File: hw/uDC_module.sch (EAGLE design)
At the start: 38 parts, among them J1 GROVE-4P-2.0-3470130P1, J2 GROVE-4P-2.0-3470130P1, U5 LD3985XX, X1 22-23-2021, X2 22-23-2021, X3 53047-06, X4 53047-06

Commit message: layout completed
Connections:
- new net ANALOG: U$6.PA2, X4-6.S
- new net ENC_A: U$6.PB6, X4-3.S
- new net ENC_B: U$6.PB7, X4-4.S
- new net ENC_I: U$6.PB5, X4-5.S
- new net LIMIT_A: U$6.PA3, X3-1.S
- new net LIMIT_B: U$6.PA4, X3-3.S
- new net STOP: U$6.PA5, X3-5.S
- net +5V: now also X4-1.S
- net GND: now also X3-2.S, X3-4.S, X3-6.S, X4-2.S
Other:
- moved on the sheet: X3-1, X3-2, X3-3, X3-4, X3-5, X3-6
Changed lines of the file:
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@@
 <part name="ZD1" library="dp_devices" deviceset="ZENER" device="SOD-323F"/>
 <part name="GND27" library="supply" deviceset="GND" device=""/>
+<part name="GND32" library="supply1" deviceset="GND" device=""/>
+<part name="P+4" library="supply" deviceset="+5V" device=""/>
+<part name="GND33" library="supply1" deviceset="GND" device=""/>
 </parts>
 <sheets>
@@
 <instance part="X2" gate="-1" x="317.5" y="127"/>
 <instance part="X2" gate="-2" x="317.5" y="124.46"/>
-<instance part="X3" gate="-1" x="271.78" y="124.46"/>
-<instance part="X3" gate="-2" x="271.78" y="121.92"/>
-<instance part="X3" gate="-3" x="271.78" y="119.38"/>
-<instance part="X3" gate="-4" x="271.78" y="116.84"/>
-<instance part="X3" gate="-5" x="271.78" y="114.3"/>
-<instance part="X3" gate="-6" x="271.78" y="111.76"/>
+<instance part="X3" gate="-1" x="281.94" y="109.22"/>
+<instance part="X3" gate="-2" x="281.94" y="106.68"/>
+<instance part="X3" gate="-3" x="281.94" y="104.14"/>
+<instance part="X3" gate="-4" x="281.94" y="101.6"/>
+<instance part="X3" gate="-5" x="281.94" y="99.06"/>
+<instance part="X3" gate="-6" x="281.94" y="96.52"/>
 <instance part="C12" gate="G$1" x="248.92" y="198.12"/>
 <instance part="GND18" gate="1" x="304.8" y="137.16"/>
@@
 <instance part="ZD1" gate="G$1" x="180.34" y="170.18" rot="R90"/>
 <instance part="GND27" gate="1" x="180.34" y="162.56"/>
+<instance part="GND32" gate="1" x="228.6" y="91.44"/>
+<instance part="P+4" gate="1" x="228.6" y="116.84"/>
+<instance part="GND33" gate="1" x="276.86" y="91.44"/>
 </instances>
 <busses>
@@
 <pinref part="GND27" gate="1" pin="GND"/>
 <wire x1="180.34" y1="167.64" x2="180.34" y2="165.1" width="0.1524" layer="91"/>
+</segment>
+<segment>
+<pinref part="X4" gate="-2" pin="S"/>
+<wire x1="231.14" y1="106.68" x2="228.6" y2="106.68" width="0.1524" layer="91"/>
+<wire x1="228.6" y1="106.68" x2="228.6" y2="93.98" width="0.1524" layer="91"/>
+<pinref part="GND32" gate="1" pin="GND"/>
+</segment>
+<segment>
+<pinref part="X3" gate="-2" pin="S"/>
+<wire x1="279.4" y1="106.68" x2="276.86" y2="106.68" width="0.1524" layer="91"/>
+<wire x1="276.86" y1="106.68" x2="276.86" y2="101.6" width="0.1524" layer="91"/>
+<pinref part="X3" gate="-4" pin="S"/>
+<wire x1="276.86" y1="101.6" x2="276.86" y2="96.52" width="0.1524" layer="91"/>
+<wire x1="276.86" y1="96.52" x2="276.86" y2="93.98" width="0.1524" layer="91"/>
+<wire x1="279.4" y1="101.6" x2="276.86" y2="101.6" width="0.1524" layer="91"/>
+<junction x="276.86" y="101.6"/>
+<pinref part="X3" gate="-6" pin="S"/>
+<wire x1="279.4" y1="96.52" x2="276.86" y2="96.52" width="0.1524" layer="91"/>
+<junction x="276.86" y="96.52"/>
+<pinref part="GND33" gate="1" pin="GND"/>
 </segment>
 </net>
@@
 <pinref part="P+3" gate="1" pin="+5V"/>
 </segment>
+<segment>
+<pinref part="X4" gate="-1" pin="S"/>
+<wire x1="231.14" y1="109.22" x2="228.6" y2="109.22" width="0.1524" layer="91"/>
+<wire x1="228.6" y1="109.22" x2="228.6" y2="114.3" width="0.1524" layer="91"/>
+<pinref part="P+4" gate="1" pin="+5V"/>
+</segment>
 </net>
 <net name="D1" class="0">
@@
 </segment>
 </net>
+<net name="ENC_A" class="0">
+<segment>
+<pinref part="X4" gate="-3" pin="S"/>
+<wire x1="231.14" y1="104.14" x2="226.06" y2="104.14" width="0.1524" layer="91"/>
+<label x="226.06" y="104.14" size="1.778" layer="95" rot="MR0"/>
+</segment>
+<segment>
+<pinref part="U$6" gate="G$1" pin="PB6"/>
+<wire x1="83.82" y1="208.28" x2="86.36" y2="208.28" width="0.1524" layer="91"/>
+<label x="86.36" y="208.28" size="1.778" layer="95"/>
+</segment>
+</net>
+<net name="ENC_B" class="0">
+<segment>
+<pinref part="X4" gate="-4" pin="S"/>
+<wire x1="231.14" y1="101.6" x2="226.06" y2="101.6" width="0.1524" layer="91"/>
+<label x="226.06" y="101.6" size="1.778" layer="95" rot="MR0"/>
+</segment>
+<segment>
+<pinref part="U$6" gate="G$1" pin="PB7"/>
+<wire x1="83.82" y1="210.82" x2="86.36" y2="210.82" width="0.1524" layer="91"/>
+<label x="86.36" y="210.82" size="1.778" layer="95"/>
+</segment>
+</net>
+<net name="ENC_I" class="0">
+<segment>
+<pinref part="X4" gate="-5" pin="S"/>
+<wire x1="231.14" y1="99.06" x2="226.06" y2="99.06" width="0.1524" layer="91"/>
+<label x="226.06" y="99.06" size="1.778" layer="95" rot="MR0"/>
+</segment>
+<segment>
+<pinref part="U$6" gate="G$1" pin="PB5"/>
+<wire x1="83.82" y1="205.74" x2="86.36" y2="205.74" width="0.1524" layer="91"/>
+<label x="86.36" y="205.74" size="1.778" layer="95"/>
+</segment>
+</net>
+<net name="ANALOG" class="0">
+<segment>
+<pinref part="X4" gate="-6" pin="S"/>
+<wire x1="231.14" y1="96.52" x2="226.06" y2="96.52" width="0.1524" layer="91"/>
+<label x="226.06" y="96.52" size="1.778" layer="95" rot="MR0"/>
+</segment>
+<segment>
+<pinref part="U$6" gate="G$1" pin="PA2"/>
+<wire x1="25.4" y1="195.58" x2="22.86" y2="195.58" width="0.1524" layer="91"/>
+<label x="22.86" y="195.58" size="1.778" layer="95" rot="MR0"/>
+</segment>
+</net>
+<net name="STOP" class="0">
+<segment>
+<pinref part="X3" gate="-5" pin="S"/>
+<wire x1="279.4" y1="99.06" x2="274.32" y2="99.06" width="0.1524" layer="91"/>
+<label x="274.32" y="99.06" size="1.778" layer="95" rot="MR0"/>
+</segment>
+<segment>
+<pinref part="U$6" gate="G$1" pin="PA5"/>
+<wire x1="43.18" y1="177.8" x2="43.18" y2="175.26" width="0.1524" layer="91"/>
+<label x="43.18" y="175.26" size="1.778" layer="95" rot="MR270"/>
+</segment>
+</net>
+<net name="LIMIT_B" class="0">
+<segment>
+<pinref part="X3" gate="-3" pin="S"/>
+<wire x1="279.4" y1="104.14" x2="274.32" y2="104.14" width="0.1524" layer="91"/>
+<label x="274.32" y="104.14" size="1.778" layer="95" rot="MR0"/>
+</segment>
+<segment>
+<pinref part="U$6" gate="G$1" pin="PA4"/>
+<wire x1="40.64" y1="177.8" x2="40.64" y2="175.26" width="0.1524" layer="91"/>
+<label x="40.64" y="175.26" size="1.778" layer="95" rot="MR270"/>
+</segment>
+</net>
+<net name="LIMIT_A" class="0">
+<segment>
+<pinref part="X3" gate="-1" pin="S"/>
+<wire x1="279.4" y1="109.22" x2="274.32" y2="109.22" width="0.1524" layer="91"/>
+<label x="274.32" y="109.22" size="1.778" layer="95" rot="MR0"/>
+</segment>
+<segment>
+<pinref part="U$6" gate="G$1" pin="PA3"/>
+<wire x1="25.4" y1="193.04" x2="22.86" y2="193.04" width="0.1524" layer="91"/>
+<label x="22.86" y="193.04" size="1.778" layer="95" rot="MR0"/>
+</segment>
+</net>

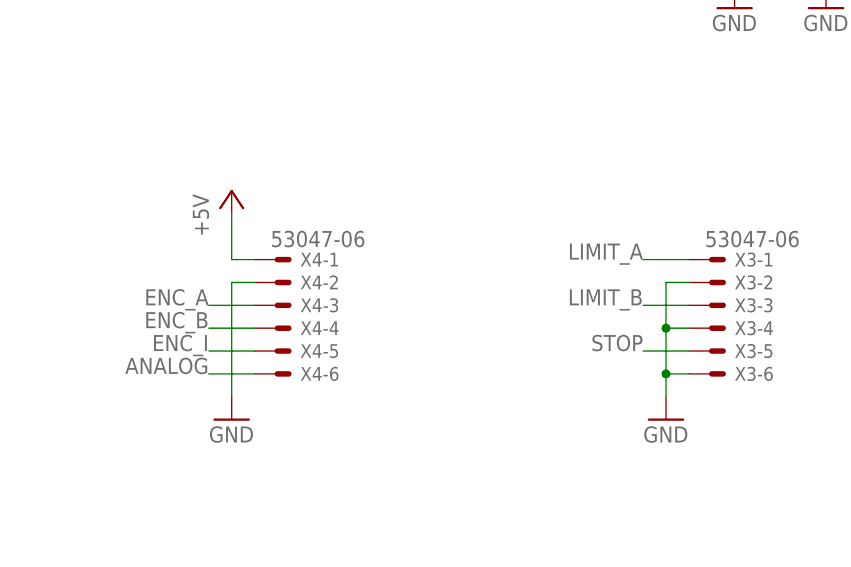
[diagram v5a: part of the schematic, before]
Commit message: updated all connectors to have GND on pin 1
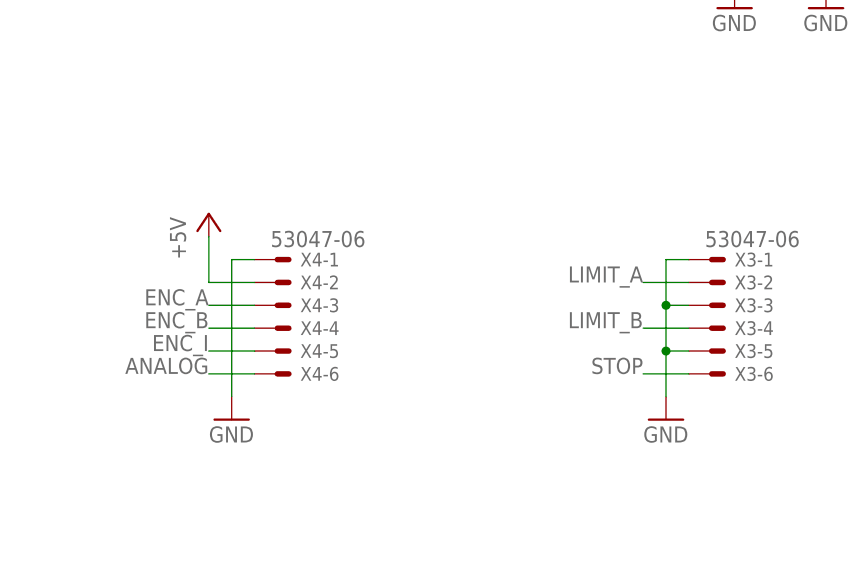
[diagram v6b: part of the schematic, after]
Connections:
- net +5V: now also X4-2.S; no longer X4-1.S
- net GND: now also X3-1.S, X3-3.S, X3-5.S, X4-1.S; no longer X3-2.S, X3-4.S, X3-6.S, X4-2.S
- net LIMIT_A: now also X3-2.S; no longer X3-1.S
- net LIMIT_B: now also X3-4.S; no longer X3-3.S
- net STOP: now also X3-6.S; no longer X3-5.S
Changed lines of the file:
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@@
 <instance part="GND27" gate="1" x="180.34" y="162.56"/>
 <instance part="GND32" gate="1" x="228.6" y="91.44"/>
-<instance part="P+4" gate="1" x="228.6" y="116.84"/>
+<instance part="P+4" gate="1" x="226.06" y="114.3"/>
 <instance part="GND33" gate="1" x="276.86" y="91.44"/>
 </instances>
@@
 </segment>
 <segment>
-<pinref part="X4" gate="-2" pin="S"/>
-<wire x1="231.14" y1="106.68" x2="228.6" y2="106.68" width="0.1524" layer="91"/>
 <wire x1="228.6" y1="106.68" x2="228.6" y2="93.98" width="0.1524" layer="91"/>
 <pinref part="GND32" gate="1" pin="GND"/>
-</segment>
-<segment>
-<pinref part="X3" gate="-2" pin="S"/>
-<wire x1="279.4" y1="106.68" x2="276.86" y2="106.68" width="0.1524" layer="91"/>
-<wire x1="276.86" y1="106.68" x2="276.86" y2="101.6" width="0.1524" layer="91"/>
-<pinref part="X3" gate="-4" pin="S"/>
-<wire x1="276.86" y1="101.6" x2="276.86" y2="96.52" width="0.1524" layer="91"/>
+<pinref part="X4" gate="-1" pin="S"/>
+<wire x1="231.14" y1="109.22" x2="228.6" y2="109.22" width="0.1524" layer="91"/>
+<wire x1="228.6" y1="109.22" x2="228.6" y2="106.68" width="0.1524" layer="91"/>
+</segment>
+<segment>
+<wire x1="276.86" y1="109.22" x2="276.86" y2="104.14" width="0.1524" layer="91"/>
+<wire x1="276.86" y1="104.14" x2="276.86" y2="101.6" width="0.1524" layer="91"/>
+<wire x1="276.86" y1="101.6" x2="276.86" y2="99.06" width="0.1524" layer="91"/>
+<wire x1="276.86" y1="99.06" x2="276.86" y2="96.52" width="0.1524" layer="91"/>
 <wire x1="276.86" y1="96.52" x2="276.86" y2="93.98" width="0.1524" layer="91"/>
-<wire x1="279.4" y1="101.6" x2="276.86" y2="101.6" width="0.1524" layer="91"/>
-<junction x="276.86" y="101.6"/>
-<pinref part="X3" gate="-6" pin="S"/>
-<wire x1="279.4" y1="96.52" x2="276.86" y2="96.52" width="0.1524" layer="91"/>
-<junction x="276.86" y="96.52"/>
 <pinref part="GND33" gate="1" pin="GND"/>
+<pinref part="X3" gate="-1" pin="S"/>
+<wire x1="279.4" y1="109.22" x2="276.86" y2="109.22" width="0.1524" layer="91"/>
+<pinref part="X3" gate="-3" pin="S"/>
+<wire x1="279.4" y1="104.14" x2="276.86" y2="104.14" width="0.1524" layer="91"/>
+<junction x="276.86" y="104.14"/>
+<pinref part="X3" gate="-5" pin="S"/>
+<wire x1="279.4" y1="99.06" x2="276.86" y2="99.06" width="0.1524" layer="91"/>
+<junction x="276.86" y="99.06"/>
 </segment>
 </net>
@@
 </segment>
 <segment>
-<pinref part="X4" gate="-1" pin="S"/>
-<wire x1="231.14" y1="109.22" x2="228.6" y2="109.22" width="0.1524" layer="91"/>
-<wire x1="228.6" y1="109.22" x2="228.6" y2="114.3" width="0.1524" layer="91"/>
+<wire x1="226.06" y1="106.68" x2="226.06" y2="111.76" width="0.1524" layer="91"/>
 <pinref part="P+4" gate="1" pin="+5V"/>
+<pinref part="X4" gate="-2" pin="S"/>
+<wire x1="226.06" y1="106.68" x2="231.14" y2="106.68" width="0.1524" layer="91"/>
 </segment>
 </net>
@@
 <net name="STOP" class="0">
 <segment>
-<pinref part="X3" gate="-5" pin="S"/>
-<wire x1="279.4" y1="99.06" x2="274.32" y2="99.06" width="0.1524" layer="91"/>
-<label x="274.32" y="99.06" size="1.778" layer="95" rot="MR0"/>
+<wire x1="279.4" y1="96.52" x2="274.32" y2="96.52" width="0.1524" layer="91"/>
+<label x="274.32" y="96.52" size="1.778" layer="95" rot="MR0"/>
+<pinref part="X3" gate="-6" pin="S"/>
 </segment>
 <segment>
@@
 <net name="LIMIT_B" class="0">
 <segment>
-<pinref part="X3" gate="-3" pin="S"/>
-<wire x1="279.4" y1="104.14" x2="274.32" y2="104.14" width="0.1524" layer="91"/>
-<label x="274.32" y="104.14" size="1.778" layer="95" rot="MR0"/>
+<wire x1="279.4" y1="101.6" x2="274.32" y2="101.6" width="0.1524" layer="91"/>
+<label x="274.32" y="101.6" size="1.778" layer="95" rot="MR0"/>
+<pinref part="X3" gate="-4" pin="S"/>
 </segment>
 <segment>
@@
 <net name="LIMIT_A" class="0">
 <segment>
-<pinref part="X3" gate="-1" pin="S"/>
-<wire x1="279.4" y1="109.22" x2="274.32" y2="109.22" width="0.1524" layer="91"/>
-<label x="274.32" y="109.22" size="1.778" layer="95" rot="MR0"/>
-</segment>
-<segment>
+<wire x1="279.4" y1="106.68" x2="274.32" y2="106.68" width="0.1524" layer="91"/>
+<label x="274.32" y="106.68" size="1.778" layer="95" rot="MR0"/>
+<pinref part="X3" gate="-2" pin="S"/>
+</segment>
+<segment>

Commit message: final revision
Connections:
- net +5V: now also X4-1.S; no longer X4-2.S
- net GND: now also X3-2.S, X3-4.S, X3-6.S, X4-2.S; no longer X3-1.S, X3-3.S, X3-5.S, X4-1.S
- net LIMIT_A: now also X3-1.S; no longer X3-2.S
- net LIMIT_B: now also X3-3.S; no longer X3-4.S
- net STOP: now also X3-5.S; no longer X3-6.S
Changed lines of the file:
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@@
 <instance part="GND27" gate="1" x="180.34" y="162.56"/>
 <instance part="GND32" gate="1" x="228.6" y="91.44"/>
-<instance part="P+4" gate="1" x="226.06" y="114.3"/>
+<instance part="P+4" gate="1" x="228.6" y="116.84"/>
 <instance part="GND33" gate="1" x="276.86" y="91.44"/>
 </instances>
@@
 <wire x1="228.6" y1="106.68" x2="228.6" y2="93.98" width="0.1524" layer="91"/>
 <pinref part="GND32" gate="1" pin="GND"/>
-<pinref part="X4" gate="-1" pin="S"/>
-<wire x1="231.14" y1="109.22" x2="228.6" y2="109.22" width="0.1524" layer="91"/>
-<wire x1="228.6" y1="109.22" x2="228.6" y2="106.68" width="0.1524" layer="91"/>
-</segment>
-<segment>
-<wire x1="276.86" y1="109.22" x2="276.86" y2="104.14" width="0.1524" layer="91"/>
+<pinref part="X4" gate="-2" pin="S"/>
+<wire x1="231.14" y1="106.68" x2="228.6" y2="106.68" width="0.1524" layer="91"/>
+</segment>
+<segment>
+<wire x1="276.86" y1="106.68" x2="276.86" y2="104.14" width="0.1524" layer="91"/>
 <wire x1="276.86" y1="104.14" x2="276.86" y2="101.6" width="0.1524" layer="91"/>
 <wire x1="276.86" y1="101.6" x2="276.86" y2="99.06" width="0.1524" layer="91"/>
@@
 <wire x1="276.86" y1="96.52" x2="276.86" y2="93.98" width="0.1524" layer="91"/>
 <pinref part="GND33" gate="1" pin="GND"/>
-<pinref part="X3" gate="-1" pin="S"/>
-<wire x1="279.4" y1="109.22" x2="276.86" y2="109.22" width="0.1524" layer="91"/>
-<pinref part="X3" gate="-3" pin="S"/>
-<wire x1="279.4" y1="104.14" x2="276.86" y2="104.14" width="0.1524" layer="91"/>
-<junction x="276.86" y="104.14"/>
-<pinref part="X3" gate="-5" pin="S"/>
-<wire x1="279.4" y1="99.06" x2="276.86" y2="99.06" width="0.1524" layer="91"/>
-<junction x="276.86" y="99.06"/>
+<pinref part="X3" gate="-2" pin="S"/>
+<wire x1="279.4" y1="106.68" x2="276.86" y2="106.68" width="0.1524" layer="91"/>
+<pinref part="X3" gate="-4" pin="S"/>
+<wire x1="279.4" y1="101.6" x2="276.86" y2="101.6" width="0.1524" layer="91"/>
+<junction x="276.86" y="101.6"/>
+<pinref part="X3" gate="-6" pin="S"/>
+<wire x1="279.4" y1="96.52" x2="276.86" y2="96.52" width="0.1524" layer="91"/>
+<junction x="276.86" y="96.52"/>
 </segment>
 </net>
@@
 </segment>
 <segment>
-<wire x1="226.06" y1="106.68" x2="226.06" y2="111.76" width="0.1524" layer="91"/>
+<wire x1="228.6" y1="109.22" x2="228.6" y2="114.3" width="0.1524" layer="91"/>
 <pinref part="P+4" gate="1" pin="+5V"/>
-<pinref part="X4" gate="-2" pin="S"/>
-<wire x1="226.06" y1="106.68" x2="231.14" y2="106.68" width="0.1524" layer="91"/>
+<pinref part="X4" gate="-1" pin="S"/>
+<wire x1="231.14" y1="109.22" x2="228.6" y2="109.22" width="0.1524" layer="91"/>
 </segment>
 </net>
@@
 <net name="STOP" class="0">
 <segment>
-<wire x1="279.4" y1="96.52" x2="274.32" y2="96.52" width="0.1524" layer="91"/>
-<label x="274.32" y="96.52" size="1.778" layer="95" rot="MR0"/>
-<pinref part="X3" gate="-6" pin="S"/>
+<wire x1="279.4" y1="99.06" x2="274.32" y2="99.06" width="0.1524" layer="91"/>
+<label x="274.32" y="99.06" size="1.778" layer="95" rot="MR0"/>
+<pinref part="X3" gate="-5" pin="S"/>
 </segment>
 <segment>
@@
 <net name="LIMIT_B" class="0">
 <segment>
-<wire x1="279.4" y1="101.6" x2="274.32" y2="101.6" width="0.1524" layer="91"/>
-<label x="274.32" y="101.6" size="1.778" layer="95" rot="MR0"/>
-<pinref part="X3" gate="-4" pin="S"/>
+<wire x1="279.4" y1="104.14" x2="274.32" y2="104.14" width="0.1524" layer="91"/>
+<label x="274.32" y="104.14" size="1.778" layer="95" rot="MR0"/>
+<pinref part="X3" gate="-3" pin="S"/>
 </segment>
 <segment>
@@
 <net name="LIMIT_A" class="0">
 <segment>
-<wire x1="279.4" y1="106.68" x2="274.32" y2="106.68" width="0.1524" layer="91"/>
-<label x="274.32" y="106.68" size="1.778" layer="95" rot="MR0"/>
-<pinref part="X3" gate="-2" pin="S"/>
-</segment>
-<segment>
+<wire x1="279.4" y1="109.22" x2="274.32" y2="109.22" width="0.1524" layer="91"/>
+<label x="274.32" y="109.22" size="1.778" layer="95" rot="MR0"/>
+<pinref part="X3" gate="-1" pin="S"/>
+</segment>
+<segment>
